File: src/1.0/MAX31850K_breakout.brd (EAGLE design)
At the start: 20 x 20 mm, 15 parts, among them J1 M08SQ1, U1 3.3V, U2 MAX31850K

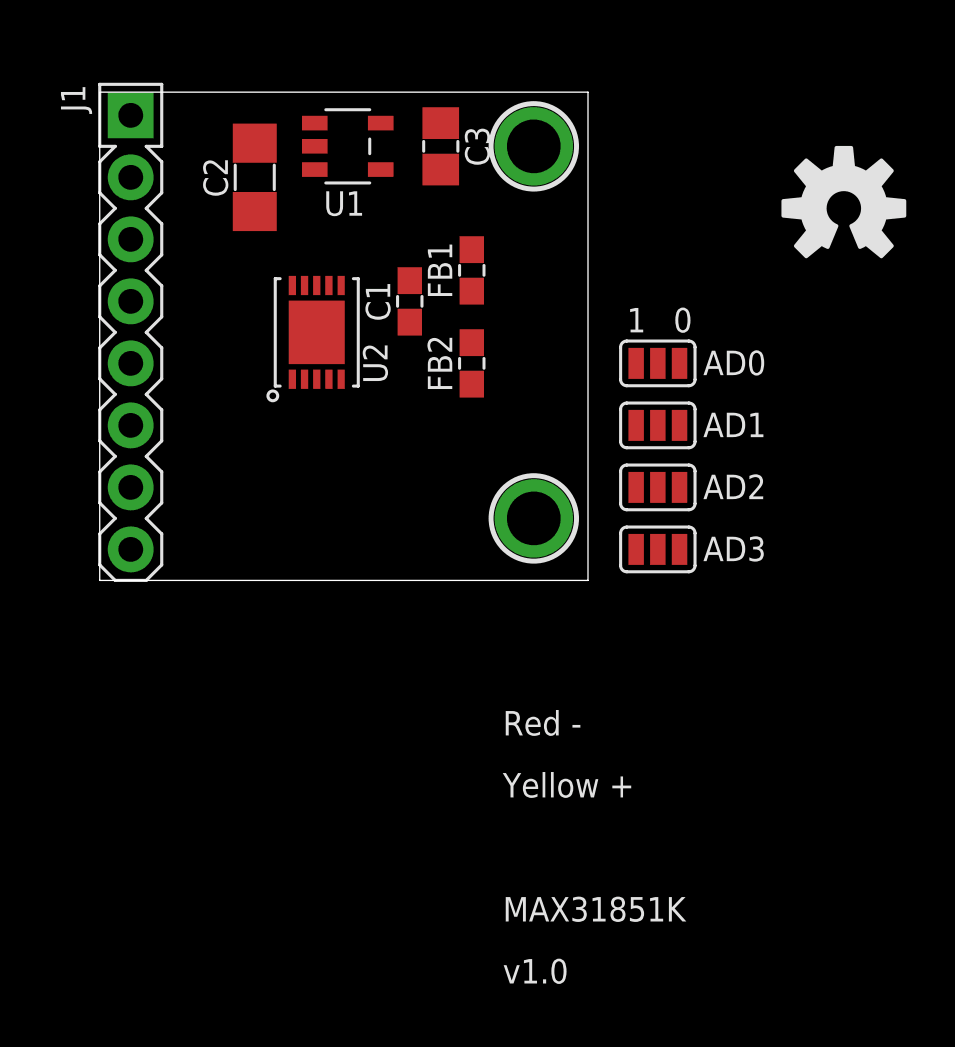
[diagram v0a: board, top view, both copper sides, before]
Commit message: Updated file structure to match PCBGuidelines structure (still in development). Preparing to move to release candidate.
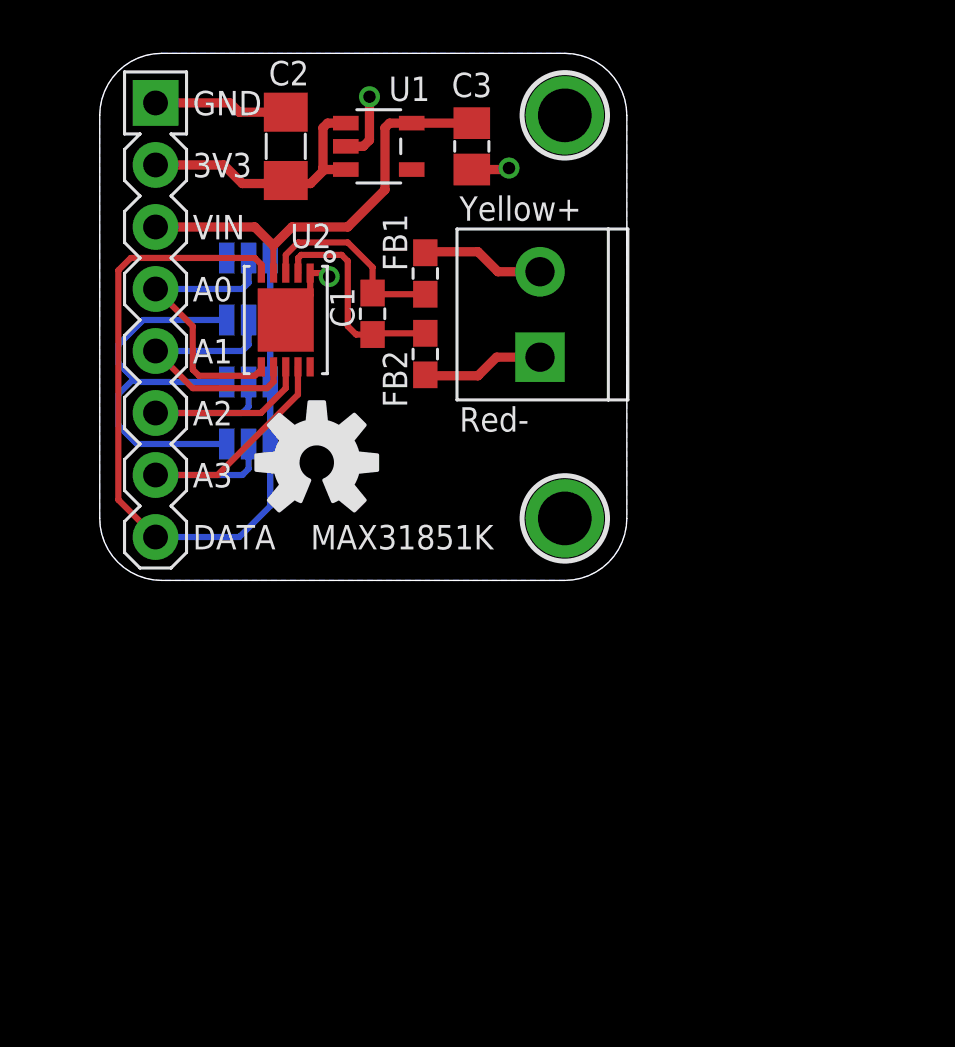
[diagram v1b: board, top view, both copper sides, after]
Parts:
- added J2: M02ST-3.5MM, LoganSmith-Connectors:SCREWTERMINAL-3.5MM-2
- moved LOGO1 24.0 mm to (8.89, 4.83)
- moved AD0 17.3 mm to (6.10, 13.2), flipped to the bottom
- moved AD1 17.3 mm to (6.10, 10.7), flipped to the bottom
- moved AD2 17.3 mm to (6.10, 8.13), flipped to the bottom
- moved AD3 17.3 mm to (6.10, 5.59), flipped to the bottom
- moved FB2 1.94 mm to (13.3, 9.27)
- moved FB1 1.91 mm to (13.3, 12.6), turned to 270 degrees
- moved C2 1.80 mm to (7.62, 17.8)
- moved U$2 1.80 mm to (19.1, 19.1)
- moved C1 1.61 mm to (11.2, 10.9), turned to 270 degrees
- moved U2 1.37 mm to (7.62, 10.7), turned to 270 degrees
- moved C3 1.27 mm to (15.2, 17.8)
- moved U$1 1.27 mm to (19.1, 2.54)
- moved U1 1.27 mm to (11.4, 17.8)
- moved J1 1.14 mm to (2.29, 19.6)
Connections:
- new net TM_RAW: FB2.P$1, J2.1
- new net TP_RAW: FB1.P$1, J2.2
- net GND: no longer U$1.P$1, U$2.P$1
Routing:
- net DATA: track 0.00 -> 33.5 mm
- net GND: track 0.00 -> 30.4 mm, vias 0 -> 3
- net +3V3: track 0.00 -> 18.0 mm
- net AD3: track 0.00 -> 13.3 mm
- net AD0: track 0.00 -> 12.0 mm
- net AD2: track 0.00 -> 11.6 mm
- net VIN: track 0.00 -> 11.2 mm
- net AD1: track 0.00 -> 11.1 mm
- net TM_FILT: track 0.00 -> 8.82 mm
- net TP_FILT: track 0.00 -> 8.17 mm
- net TP_RAW: track 0.00 -> 5.05 mm
- net TM_RAW: track 0.00 -> 5.03 mm
- added copper zone on layer 16, net GND
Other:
- board size 20 x 20 mm -> 21.6 x 21.6 mm
- board text added: "3V3"
- board text added: "A0"
- board text added: "A1"
- board text added: "A2"
- board text added: "A3"
- board text added: "DATA"
- board text added: "GND"
- board text added: "Logan Smith"
- board text added: "Red-"
- board text added: "VIN"
- board text added: "VIN: 3.6-16V DATA: 3.3V"
- board text added: "Yellow+"
- board text removed: "Red -"
- board text removed: "Yellow +"

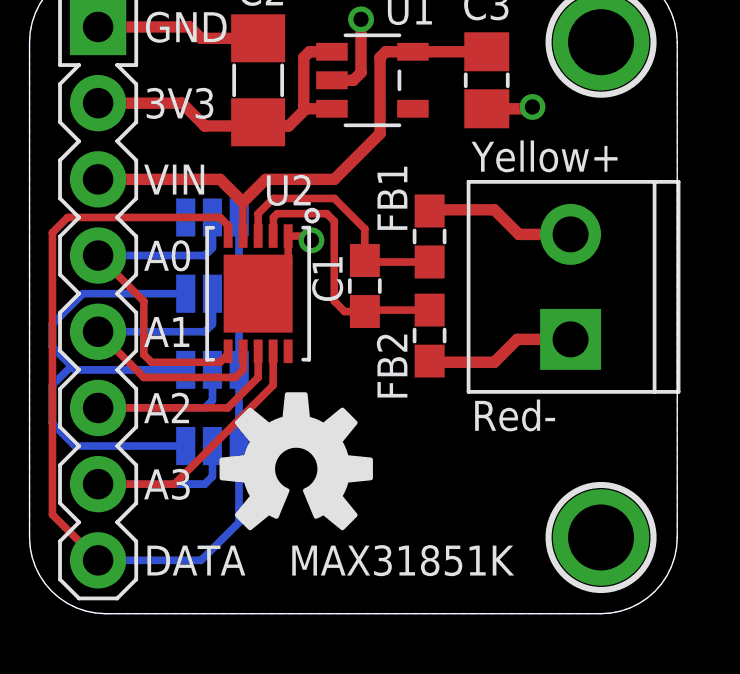
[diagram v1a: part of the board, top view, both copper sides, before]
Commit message: Slighly rearranged silk.
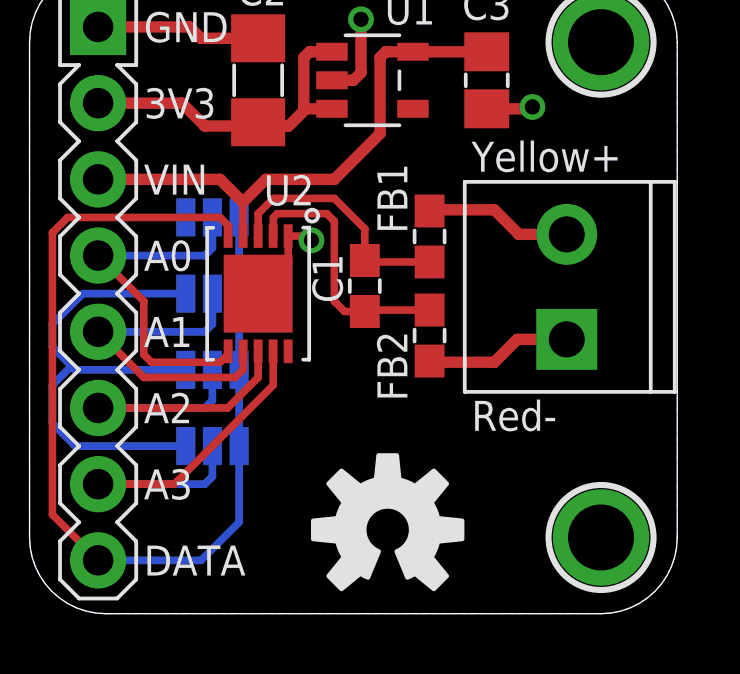
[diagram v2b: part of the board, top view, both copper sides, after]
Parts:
- moved LOGO1 3.66 mm to (11.9, 2.79)
- moved J2 0.13 mm to (17.9, 9.14)
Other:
- board text removed: "Logan Smith"
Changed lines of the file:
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@@
 <text x="14.732" y="6.096" size="1" layer="21" font="vector" ratio="12">Red-</text>
 <text x="14.732" y="14.732" size="1" layer="21" font="vector" ratio="12">Yellow+</text>
-<text x="8.636" y="1.27" size="1" layer="21" font="vector" ratio="12">MAX31851K</text>
+<text x="15.24" y="1.016" size="1.25" layer="22" font="vector" ratio="12" rot="MR0">MAX31851K</text>
 <text x="20.828" y="12.7" size="1" layer="22" font="vector" ratio="12" rot="MR270">v1.0</text>
 <wire x1="0" y1="2.54" x2="0" y2="19.05" width="0.0254" layer="20"/>
@@
 <text x="14.986" y="16.51" size="1" layer="22" ratio="12" rot="MR0">VIN: 3.6-16V
 DATA: 3.3V</text>
-<text x="16.256" y="1.016" size="1.27" layer="22" font="vector" rot="MR0">Logan Smith</text>
 </plain>
 <attributes>
@@
 <attribute name="VALUE" x="4.191" y="20.828" size="1" layer="27" font="vector" ratio="12" rot="R270"/>
 </element>
-<element name="LOGO1" library="SparkFun-Aesthetics" package="OSHW-LOGO-M" value="OSHW-LOGOM" x="8.89" y="4.826"/>
+<element name="LOGO1" library="SparkFun-Aesthetics" package="OSHW-LOGO-M" value="OSHW-LOGOM" x="11.938" y="2.794"/>
 <element name="AD0" library="LoganSmith-Connectors" package="SJ_3" value="" x="6.096" y="13.208" smashed="yes" rot="MR0">
 <attribute name="NAME" x="10.587" y="12.727" size="1" layer="26" font="vector" ratio="12" rot="MR0"/>
@@
 <element name="U$1" library="LoganSmith-Electromechanical" package="MOUNTINGHOLE_2.0_PLATED" value="MNTHOLE-2.0" x="19.05" y="2.54"/>
 <element name="U$2" library="LoganSmith-Electromechanical" package="MOUNTINGHOLE_2.0_PLATED" value="MNTHOLE-2.0" x="19.05" y="19.05"/>
-<element name="J2" library="LoganSmith-Connectors" package="SCREWTERMINAL-3.5MM-2" value="M02ST-3.5MM" x="18.034" y="9.144" smashed="yes" rot="R90">
-<attribute name="VALUE" x="20.039" y="8.149" size="0.5" layer="27" font="vector" ratio="12" rot="R90"/>
+<element name="J2" library="LoganSmith-Connectors" package="SCREWTERMINAL-3.5MM-2" value="M02ST-3.5MM" x="17.907" y="9.144" smashed="yes" rot="R90">
+<attribute name="VALUE" x="19.912" y="8.149" size="0.5" layer="27" font="vector" ratio="12" rot="R90"/>
 </element>
 </elements>
@@
 <contactref element="FB1" pad="P$1"/>
 <contactref element="J2" pad="2"/>
-<wire x1="18.034" y1="12.644" x2="16.312" y2="12.644" width="0.381" layer="1"/>
+<wire x1="17.907" y1="12.644" x2="16.312" y2="12.644" width="0.381" layer="1"/>
 <wire x1="16.312" y1="12.644" x2="15.494" y2="13.462" width="0.381" layer="1"/>
 <wire x1="15.494" y1="13.462" x2="13.374" y2="13.462" width="0.381" layer="1"/>
@@
 <contactref element="FB2" pad="P$1"/>
 <contactref element="J2" pad="1"/>
-<wire x1="18.034" y1="9.144" x2="16.256" y2="9.144" width="0.381" layer="1"/>
+<wire x1="17.907" y1="9.144" x2="16.256" y2="9.144" width="0.381" layer="1"/>
 <wire x1="16.256" y1="9.144" x2="15.494" y2="8.382" width="0.381" layer="1"/>
 <wire x1="15.494" y1="8.382" x2="13.374" y2="8.382" width="0.381" layer="1"/>

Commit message: Added BOM, still need part number for 1x8 header.
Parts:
- U2: value MAX31850K -> Type K; device LoganSmith-Digital_IC:10-TDFN-EP -> LoganSmith-Analog_IC:10-TDFN-EP
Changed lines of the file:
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@@
 <attribute name="NAME" x="15.24" y="19.796" size="1" layer="25" font="vector" ratio="12" align="bottom-center"/>
 </element>
-<element name="U2" library="LoganSmith-Digital_IC" package="10-TDFN-EP" value="MAX31850K" x="7.62" y="10.668" smashed="yes" rot="R270">
+<element name="U2" library="LoganSmith-Analog_IC" package="10-TDFN-EP" value="Type K" x="7.62" y="10.668" smashed="yes" rot="R270">
 <attribute name="NAME" x="7.806" y="13.61" size="1" layer="25" font="vector" ratio="12"/>
-<attribute name="VALUE" x="6.42" y="7.568" size="0.5" layer="27" font="vector" ratio="12"/>
+<attribute name="VALUE" value="Type K" x="6.42" y="7.568" size="0.5" layer="27" font="vector" ratio="12"/>
+<attribute name="DESC" value="" x="7.62" y="10.668" size="1.778" layer="27" rot="R270" display="off"/>
+<attribute name="MFR" value="Maxim Integrated" x="7.62" y="10.668" size="1.778" layer="27" rot="R270" display="off"/>
+<attribute name="MPN" value="MAX31850KATB+" x="7.62" y="10.668" size="1.778" layer="27" rot="R270" display="off"/>
+<attribute name="DIGIKEY_OC" value="MAX31850KATB+-ND" x="7.62" y="10.668" size="1.778" layer="27" rot="R270" display="off"/>
 </element>
 <element name="J1" library="LoganSmith-Connectors" package="1X08_SQ1" value="M08SQ1" x="2.286" y="19.558" smashed="yes" rot="R270">
